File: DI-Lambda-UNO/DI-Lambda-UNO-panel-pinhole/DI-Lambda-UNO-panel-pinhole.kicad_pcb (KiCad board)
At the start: 2 copper layers, 33.2 x 26.6 mm, 1 part

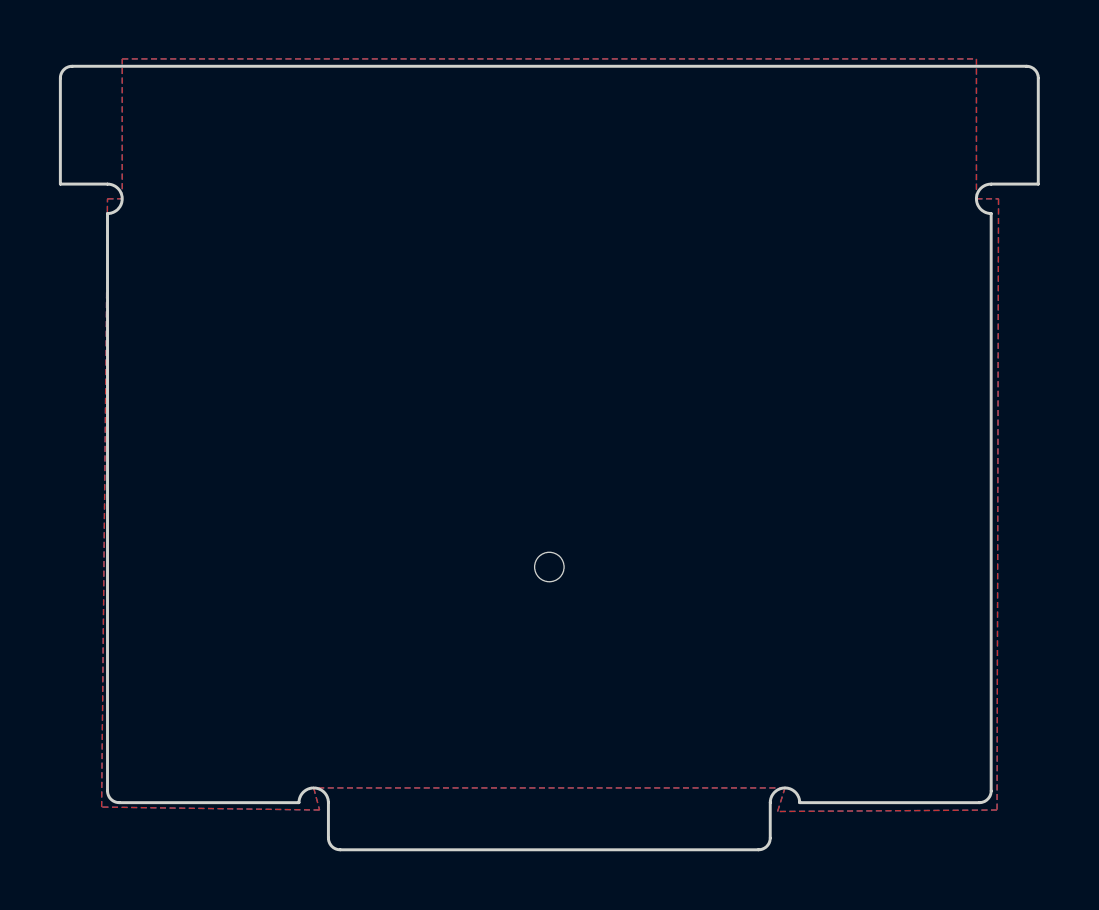
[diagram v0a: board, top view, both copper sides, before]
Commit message: Pinhole board: Convert to 18mm height
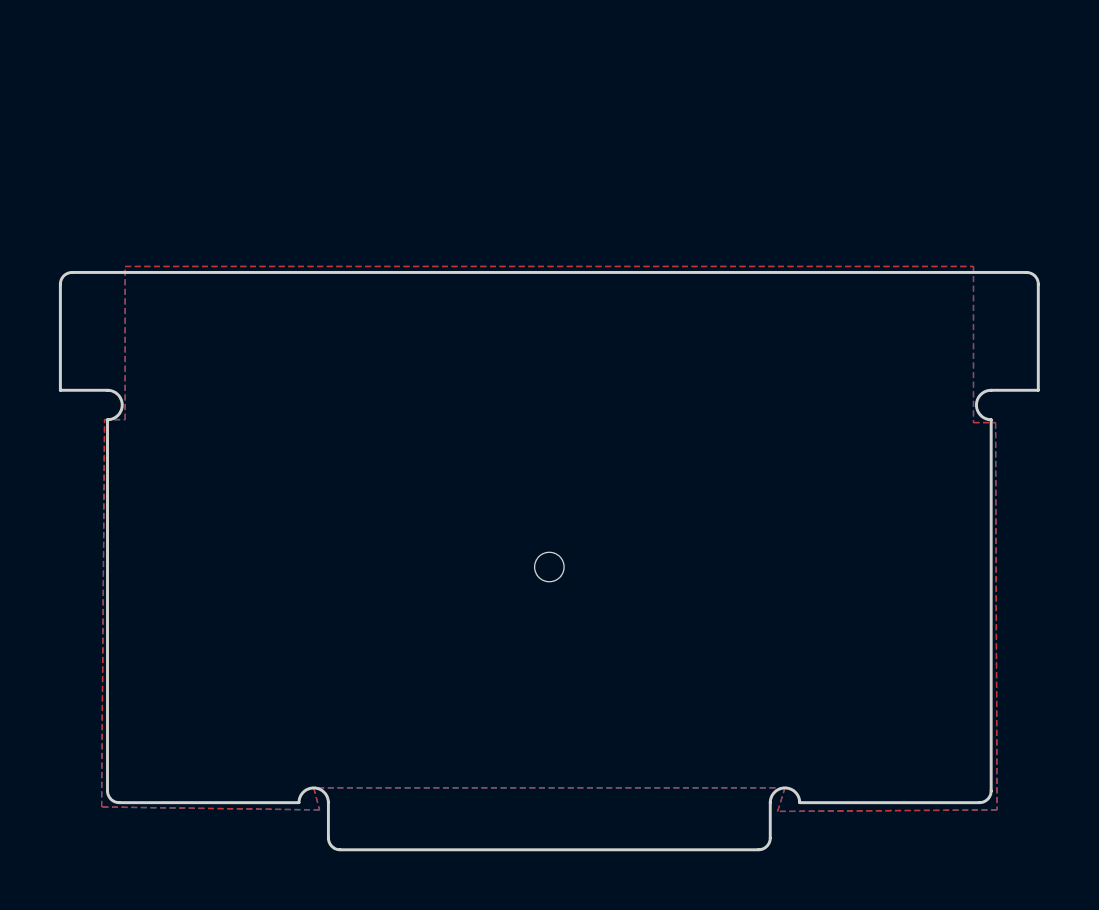
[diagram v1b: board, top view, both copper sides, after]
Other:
- board size 33.2 x 26.6 mm -> 33.2 x 19.6 mm
- board text added: "DI-Lambda UNO v1.3"
- board text removed: "DI-Lambda UNO v1.1"
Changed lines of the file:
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@@
     (pad "" np_thru_hole circle (at 0 0) (size 1 1) (drill 1) (layers *.Cu))
   )
-  (gr_text "DI-Lambda UNO v1.1" (at 160 70.8) (layer F.Mask)
+  (gr_text "DI-Lambda UNO v1.3" (at 160.2 76.4) (layer F.Mask)
     (effects (font (size 1.5 1.5) (thickness 0.3)))
   )
@@
     (arrow2b (pts (xy 156.2 92) (xy 155.613579 90.873496)))
   )
-  (gr_arc (start 175 71.5) (end 175 72) (angle 180) (layer Edge.Cuts) (width 0.1))
-  (gr_arc (start 145 71.5) (end 145 71) (angle 180) (layer Edge.Cuts) (width 0.1))
-  (gr_arc (start 176.2 67.4) (end 176.2 67) (angle 90) (layer Edge.Cuts) (width 0.1))
-  (gr_arc (start 143.8 67.4) (end 143.4 67.4) (angle 90) (layer Edge.Cuts) (width 0.1))
+  (gr_arc (start 175 78.5) (end 175 79) (angle 180) (layer Edge.Cuts) (width 0.1))
+  (gr_arc (start 145 78.5) (end 145 78) (angle 180) (layer Edge.Cuts) (width 0.1))
+  (gr_arc (start 176.2 74.4) (end 176.2 74) (angle 90) (layer Edge.Cuts) (width 0.1))
+  (gr_arc (start 143.8 74.4) (end 143.4 74.4) (angle 90) (layer Edge.Cuts) (width 0.1))
   (gr_arc (start 174.6 91.6) (end 175 91.6) (angle 90) (layer Edge.Cuts) (width 0.1))
   (gr_arc (start 145.4 91.6) (end 145.4 92) (angle 90) (layer Edge.Cuts) (width 0.1))
@@
   (gr_arc (start 168 92) (end 167.5 92) (angle 180) (layer Edge.Cuts) (width 0.1))
   (gr_arc (start 152 92) (end 151.5 92) (angle 180) (layer Edge.Cuts) (width 0.1))
-  (gr_line (start 175 91.6) (end 175 72) (layer Edge.Cuts) (width 0.1))
-  (gr_line (start 176.2 67) (end 143.8 67) (layer Edge.Cuts) (width 0.1))
-  (gr_line (start 175 71) (end 176.6 71) (layer Edge.Cuts) (width 0.1))
-  (gr_line (start 145 91.6) (end 145 72) (layer Edge.Cuts) (width 0.1))
+  (gr_line (start 175 91.6) (end 175 79) (layer Edge.Cuts) (width 0.1))
+  (gr_line (start 176.2 74) (end 143.8 74) (layer Edge.Cuts) (width 0.1))
+  (gr_line (start 175 78) (end 176.6 78) (layer Edge.Cuts) (width 0.1))
+  (gr_line (start 145 91.6) (end 145 79) (layer Edge.Cuts) (width 0.1))
   (gr_line (start 174.6 92) (end 168.5 92) (layer Edge.Cuts) (width 0.1))
-  (gr_line (start 176.6 67.4) (end 176.6 71) (layer Edge.Cuts) (width 0.1))
+  (gr_line (start 176.6 74.4) (end 176.6 78) (layer Edge.Cuts) (width 0.1))
   (gr_line (start 167.5 93.2) (end 167.5 92) (layer Edge.Cuts) (width 0.1))
   (gr_line (start 152.9 93.6) (end 167.1 93.6) (layer Edge.Cuts) (width 0.1))
-  (gr_line (start 143.4 71) (end 143.4 67.4) (layer Edge.Cuts) (width 0.1))
-  (gr_line (start 145 71) (end 143.4 71) (layer Edge.Cuts) (width 0.1))
+  (gr_line (start 143.4 78) (end 143.4 74.4) (layer Edge.Cuts) (width 0.1))
+  (gr_line (start 145 78) (end 143.4 78) (layer Edge.Cuts) (width 0.1))
   (gr_line (start 152.5 92) (end 152.5 93.2) (layer Edge.Cuts) (width 0.1))
   (gr_line (start 145.4 92) (end 151.5 92) (layer Edge.Cuts) (width 0.1))
-  (zone (net 0) (net_name "") (layer F.Cu) (hatch edge 0.508)
-    (connect_pads (clearance 0.508))
-    (min_thickness 0.254)
-    (fill yes (arc_segments 16) (thermal_gap 0.508) (thermal_bridge_width 0.508))
-    (polygon
-      (pts
-        (xy 145.5 66.75) (xy 174.5 66.75) (xy 174.5 71.5) (xy 175.25 71.5) (xy 175.2 92.25)
-        (xy 167.75 92.3) (xy 168 91.5) (xy 152 91.5) (xy 152.2 92.25) (xy 144.8 92.15)
-        (xy 145 71.5) (xy 145.5 71.5)
-      )
-    )
-  )
   (zone (net 0) (net_name "") (layer B.Cu) (hatch edge 0.508)
     (connect_pads (clearance 0.508))
@@
     (polygon
       (pts
-        (xy 145.5 66.75) (xy 174.5 66.75) (xy 174.5 71.5) (xy 175.25 71.5) (xy 175.2 92.25)
+        (xy 145.6 73.8) (xy 174.4 73.8) (xy 174.4 79.1) (xy 175.15 79.1) (xy 175.2 92.25)
         (xy 167.75 92.3) (xy 168 91.5) (xy 152 91.5) (xy 152.2 92.25) (xy 144.8 92.15)
-        (xy 145 71.5) (xy 145.5 71.5)
+        (xy 144.9 79) (xy 145.6 79)
       )
     )
@@
     (polygon
       (pts
-        (xy 147.5 69.5) (xy 172.25 69.5) (xy 172.25 72) (xy 147.5 72)
+        (xy 147.7 75.1) (xy 172.45 75.1) (xy 172.45 77.6) (xy 147.7 77.6)
       )
     )
+  )
+  (zone (net 0) (net_name "") (layer F.Cu) (hatch edge 0.508)
+    (connect_pads (clearance 0.508))
+    (min_thickness 0.254)
+    (fill yes (arc_segments 16) (thermal_gap 0.508) (thermal_bridge_width 0.508))
+    (polygon
+      (pts
+        (xy 145.6 73.792794) (xy 174.4 73.792794) (xy 174.4 79.092794) (xy 175.15 79.092794) (xy 175.2 92.242794)
+        (xy 167.75 92.292794) (xy 168 91.492794) (xy 152 91.492794) (xy 152.2 92.242794) (xy 144.8 92.142794)
+        (xy 144.9 78.992794) (xy 145.6 78.992794)
+      )
+    )

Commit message: Version 1.5
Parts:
- added MK2: Mounting_Hole, DI-Lambda-module-tabs:Tab_PINHOLE, F.Cu at (160.0, 92.0)
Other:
- board size 33.2 x 19.6 mm -> 33.2 x 25 mm
- board text added: "DI-Lambda UNO v1.5"
- board text removed: "DI-Lambda UNO v1.3"
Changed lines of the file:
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@@
-(kicad_pcb (version 20170123) (host pcbnew "(2017-09-07 revision 3b08636)-master")
+(kicad_pcb (version 20171130) (host pcbnew "(2018-01-22 revision c702646)-master")
   (general
     (thickness 1.6)
-    (drawings 26)
+    (drawings 19)
     (tracks 0)
     (zones 0)
-    (modules 1)
+    (modules 2)
     (nets 1)
   )
@@
       (layerselection 0x010f0_ffffffff)
       (usegerberextensions true)
-      (usegerberattributes true)
-      (usegerberadvancedattributes true)
+      (usegerberattributes false)
+      (usegerberadvancedattributes false)
       (creategerberjobfile true)
-      (excludeedgelayer false)
+      (excludeedgelayer true)
       (linewidth 0.100000)
       (plotframeref false)
@@
       (drillshape 0)
       (scaleselection 1)
-      (outputdirectory DI-Lambda-UNO-panel-pinhole-v1.1-gerbers-2017oct25/))
+      (outputdirectory DI-Lambda-UNO-panel-pinhole-v1.5-gerbers-2018feb07-1))
   )
   (net 0 "")
@@
     (uvia_drill 0.1)
   )
+  (module DI-Lambda-module-tabs:Tab_PINHOLE (layer F.Cu)
+    (at 160 92)
+    (fp_text reference MK2 (at 0 5.75) (layer F.SilkS) hide
+      (effects (font (size 1 1) (thickness 0.15)))
+    )
+    (fp_text value Mounting_Hole (at 0 3.5) (layer F.Fab)
+      (effects (font (size 1 1) (thickness 0.15)))
+    )
+    (fp_line (start -15 -2.5) (end -15 2.5) (layer F.Fab) (width 0.1))
+    (fp_line (start 15 -2.5) (end 15 2.5) (layer F.Fab) (width 0.1))
+    (fp_line (start -4.5 1.5) (end 4.5 1.5) (layer Edge.Cuts) (width 0.15))
+    (fp_line (start 5 1) (end 5 0) (layer Edge.Cuts) (width 0.15))
+    (fp_line (start -5 1) (end -5 0) (layer Edge.Cuts) (width 0.15))
+    (fp_arc (start -4.5 1) (end -5 1) (angle -90) (layer Edge.Cuts) (width 0.15))
+    (fp_arc (start 4.5 1) (end 4.5 1.5) (angle -90) (layer Edge.Cuts) (width 0.15))
+    (fp_arc (start -5.75 0) (end -5 0) (angle -180) (layer Edge.Cuts) (width 0.15))
+    (fp_arc (start 5.75 0) (end 6.5 0) (angle -180) (layer Edge.Cuts) (width 0.15))
+    (fp_line (start -5 -1) (end -5 2) (layer F.Fab) (width 0.1))
+    (fp_line (start 5 -1) (end 5 2) (layer F.Fab) (width 0.1))
+  )
   (module 1mm_hole:NPTH_1mm (layer F.Cu)
     (at 160 84)
@@
     (pad "" np_thru_hole circle (at 0 0) (size 1 1) (drill 1) (layers *.Cu))
   )
-  (gr_text "DI-Lambda UNO v1.3" (at 160.2 76.4) (layer F.Mask)
+  (gr_text "DI-Lambda UNO v1.5" (at 160.2 69.4) (layer F.Mask)
     (effects (font (size 1.5 1.5) (thickness 0.3)))
   )
@@
     (arrow2b (pts (xy 156.2 92) (xy 155.613579 90.873496)))
   )
-  (gr_arc (start 175 78.5) (end 175 79) (angle 180) (layer Edge.Cuts) (width 0.1))
-  (gr_arc (start 145 78.5) (end 145 78) (angle 180) (layer Edge.Cuts) (width 0.1))
-  (gr_arc (start 176.2 74.4) (end 176.2 74) (angle 90) (layer Edge.Cuts) (width 0.1))
-  (gr_arc (start 143.8 74.4) (end 143.4 74.4) (angle 90) (layer Edge.Cuts) (width 0.1))
+  (gr_arc (start 175 71.5) (end 175 72) (angle 180) (layer Edge.Cuts) (width 0.1))
+  (gr_arc (start 145 71.5) (end 145 71) (angle 180) (layer Edge.Cuts) (width 0.1))
+  (gr_arc (start 176.2 67.4) (end 176.2 67) (angle 90) (layer Edge.Cuts) (width 0.1))
+  (gr_arc (start 143.8 67.4) (end 143.4 67.4) (angle 90) (layer Edge.Cuts) (width 0.1))
   (gr_arc (start 174.6 91.6) (end 175 91.6) (angle 90) (layer Edge.Cuts) (width 0.1))
   (gr_arc (start 145.4 91.6) (end 145.4 92) (angle 90) (layer Edge.Cuts) (width 0.1))
-  (gr_arc (start 167.1 93.2) (end 167.5 93.2) (angle 90) (layer Edge.Cuts) (width 0.1))
-  (gr_arc (start 152.9 93.2) (end 152.9 93.6) (angle 90) (layer Edge.Cuts) (width 0.1))
-  (gr_arc (start 168 92) (end 167.5 92) (angle 180) (layer Edge.Cuts) (width 0.1))
-  (gr_arc (start 152 92) (end 151.5 92) (angle 180) (layer Edge.Cuts) (width 0.1))
-  (gr_line (start 175 91.6) (end 175 79) (layer Edge.Cuts) (width 0.1))
-  (gr_line (start 176.2 74) (end 143.8 74) (layer Edge.Cuts) (width 0.1))
-  (gr_line (start 175 78) (end 176.6 78) (layer Edge.Cuts) (width 0.1))
-  (gr_line (start 145 91.6) (end 145 79) (layer Edge.Cuts) (width 0.1))
-  (gr_line (start 174.6 92) (end 168.5 92) (layer Edge.Cuts) (width 0.1))
-  (gr_line (start 176.6 74.4) (end 176.6 78) (layer Edge.Cuts) (width 0.1))
-  (gr_line (start 167.5 93.2) (end 167.5 92) (layer Edge.Cuts) (width 0.1))
-  (gr_line (start 152.9 93.6) (end 167.1 93.6) (layer Edge.Cuts) (width 0.1))
-  (gr_line (start 143.4 78) (end 143.4 74.4) (layer Edge.Cuts) (width 0.1))
-  (gr_line (start 145 78) (end 143.4 78) (layer Edge.Cuts) (width 0.1))
-  (gr_line (start 152.5 92) (end 152.5 93.2) (layer Edge.Cuts) (width 0.1))
-  (gr_line (start 145.4 92) (end 151.5 92) (layer Edge.Cuts) (width 0.1))
+  (gr_line (start 175 91.6) (end 175 72) (layer Edge.Cuts) (width 0.1))
+  (gr_line (start 176.2 67) (end 143.8 67) (layer Edge.Cuts) (width 0.1))
+  (gr_line (start 175 71) (end 176.6 71) (layer Edge.Cuts) (width 0.1))
+  (gr_line (start 145 91.6) (end 145 72) (layer Edge.Cuts) (width 0.1))
+  (gr_line (start 174.6 92) (end 166.5 92) (layer Edge.Cuts) (width 0.1))
+  (gr_line (start 176.6 67.4) (end 176.6 71) (layer Edge.Cuts) (width 0.1))
+  (gr_line (start 143.4 71) (end 143.4 67.4) (layer Edge.Cuts) (width 0.1))
+  (gr_line (start 145 71) (end 143.4 71) (layer Edge.Cuts) (width 0.1))
+  (gr_line (start 145.4 92) (end 153.5 92) (layer Edge.Cuts) (width 0.1))
   (zone (net 0) (net_name "") (layer B.Cu) (hatch edge 0.508)
     (connect_pads (clearance 0.508))
@@
     (polygon
       (pts
-        (xy 145.6 73.8) (xy 174.4 73.8) (xy 174.4 79.1) (xy 175.15 79.1) (xy 175.2 92.25)
+        (xy 145.6 66.4) (xy 174.45 66.55) (xy 174.45 71.5) (xy 175.2 71.5) (xy 175.2 92.25)
         (xy 167.75 92.3) (xy 168 91.5) (xy 152 91.5) (xy 152.2 92.25) (xy 144.8 92.15)
-        (xy 144.9 79) (xy 145.6 79)
+        (xy 144.9 71.5) (xy 145.6 71.5)
       )
     )
@@
     (polygon
       (pts
-        (xy 147.7 75.1) (xy 172.45 75.1) (xy 172.45 77.6) (xy 147.7 77.6)
+        (xy 147.7 68.1) (xy 172.45 68.1) (xy 172.45 70.6) (xy 147.7 70.6)
       )
     )
@@
     (polygon
       (pts
-        (xy 145.6 73.792794) (xy 174.4 73.792794) (xy 174.4 79.092794) (xy 175.15 79.092794) (xy 175.2 92.242794)
+        (xy 145.65 66.55) (xy 174.45 66.55) (xy 174.45 71.5) (xy 175.2 71.5) (xy 175.2 92.242794)
         (xy 167.75 92.292794) (xy 168 91.492794) (xy 152 91.492794) (xy 152.2 92.242794) (xy 144.8 92.142794)
-        (xy 144.9 78.992794) (xy 145.6 78.992794)
+        (xy 144.95 71.5) (xy 145.65 71.5)
       )
     )

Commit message: More missing fotprints
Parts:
- moved MK1 158.3 mm to (16.6, 17.0)
- moved MK2 158.3 mm to (16.6, 25.0)
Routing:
- net (no net): vias 0 -> 1
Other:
- board text added: "DI-Lambda UNO v1.7"
- board text removed: "DI-Lambda UNO v1.5"
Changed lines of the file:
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@@
-(kicad_pcb (version 20171130) (host pcbnew "(2018-01-22 revision c702646)-master")
+(kicad_pcb (version 20171130) (host pcbnew "(5.0.0-rc2-dev-425-g1663627)")
   (general
     (thickness 1.6)
     (drawings 19)
-    (tracks 0)
+    (tracks 1)
     (zones 0)
     (modules 2)
@@
     (pad_drill 1)
     (pad_to_mask_clearance 0.2)
-    (aux_axis_origin 143.4 67)
-    (grid_origin 145 92)
+    (aux_axis_origin 0 0)
     (visible_elements FFFFFF7F)
     (pcbplotparams
@@
   )
   (module DI-Lambda-module-tabs:Tab_PINHOLE (layer F.Cu)
-    (at 160 92)
+    (at 16.6 25)
     (fp_text reference MK2 (at 0 5.75) (layer F.SilkS) hide
       (effects (font (size 1 1) (thickness 0.15)))
@@
   )
   (module 1mm_hole:NPTH_1mm (layer F.Cu)
-    (at 160 84)
+    (at 16.6 17)
     (fp_text reference MK1 (at 0 3.5) (layer F.SilkS) hide
       (effects (font (size 1 1) (thickness 0.15)))
@@
     (pad "" np_thru_hole circle (at 0 0) (size 1 1) (drill 1) (layers *.Cu))
   )
-  (gr_text "DI-Lambda UNO v1.5" (at 160.2 69.4) (layer F.Mask)
+  (gr_text "DI-Lambda UNO v1.7" (at 16.8 2.4) (layer F.Mask)
     (effects (font (size 1.5 1.5) (thickness 0.3)))
   )
@@
     (arrow2b (pts (xy 156.2 92) (xy 155.613579 90.873496)))
   )
-  (gr_arc (start 175 71.5) (end 175 72) (angle 180) (layer Edge.Cuts) (width 0.1))
-  (gr_arc (start 145 71.5) (end 145 71) (angle 180) (layer Edge.Cuts) (width 0.1))
-  (gr_arc (start 176.2 67.4) (end 176.2 67) (angle 90) (layer Edge.Cuts) (width 0.1))
-  (gr_arc (start 143.8 67.4) (end 143.4 67.4) (angle 90) (layer Edge.Cuts) (width 0.1))
-  (gr_arc (start 174.6 91.6) (end 175 91.6) (angle 90) (layer Edge.Cuts) (width 0.1))
-  (gr_arc (start 145.4 91.6) (end 145.4 92) (angle 90) (layer Edge.Cuts) (width 0.1))
-  (gr_line (start 175 91.6) (end 175 72) (layer Edge.Cuts) (width 0.1))
-  (gr_line (start 176.2 67) (end 143.8 67) (layer Edge.Cuts) (width 0.1))
-  (gr_line (start 175 71) (end 176.6 71) (layer Edge.Cuts) (width 0.1))
-  (gr_line (start 145 91.6) (end 145 72) (layer Edge.Cuts) (width 0.1))
-  (gr_line (start 174.6 92) (end 166.5 92) (layer Edge.Cuts) (width 0.1))
-  (gr_line (start 176.6 67.4) (end 176.6 71) (layer Edge.Cuts) (width 0.1))
-  (gr_line (start 143.4 71) (end 143.4 67.4) (layer Edge.Cuts) (width 0.1))
-  (gr_line (start 145 71) (end 143.4 71) (layer Edge.Cuts) (width 0.1))
-  (gr_line (start 145.4 92) (end 153.5 92) (layer Edge.Cuts) (width 0.1))
+  (gr_arc (start 31.6 4.5) (end 31.6 5) (angle 180) (layer Edge.Cuts) (width 0.1))
+  (gr_arc (start 1.6 4.5) (end 1.6 4) (angle 180) (layer Edge.Cuts) (width 0.1))
+  (gr_arc (start 32.8 0.4) (end 32.8 0) (angle 90) (layer Edge.Cuts) (width 0.1))
+  (gr_arc (start 0.4 0.4) (end 0 0.4) (angle 90) (layer Edge.Cuts) (width 0.1))
+  (gr_arc (start 31.2 24.6) (end 31.6 24.6) (angle 90) (layer Edge.Cuts) (width 0.1))
+  (gr_arc (start 2 24.6) (end 2 25) (angle 90) (layer Edge.Cuts) (width 0.1))
+  (gr_line (start 31.6 24.6) (end 31.6 5) (layer Edge.Cuts) (width 0.1))
+  (gr_line (start 32.8 0) (end 0.4 0) (layer Edge.Cuts) (width 0.1))
+  (gr_line (start 31.6 4) (end 33.2 4) (layer Edge.Cuts) (width 0.1))
+  (gr_line (start 1.6 24.6) (end 1.6 5) (layer Edge.Cuts) (width 0.1))
+  (gr_line (start 31.2 25) (end 23.1 25) (layer Edge.Cuts) (width 0.1))
+  (gr_line (start 33.2 0.4) (end 33.2 4) (layer Edge.Cuts) (width 0.1))
+  (gr_line (start 0 4) (end 0 0.4) (layer Edge.Cuts) (width 0.1))
+  (gr_line (start 1.6 4) (end 0 4) (layer Edge.Cuts) (width 0.1))
+  (gr_line (start 2 25) (end 10.1 25) (layer Edge.Cuts) (width 0.1))
+  (via (at 0 0) (size 0.8) (drill 0.4) (layers F.Cu B.Cu) (net 0))
   (zone (net 0) (net_name "") (layer B.Cu) (hatch edge 0.508)
     (connect_pads (clearance 0.508))
@@
     (polygon
       (pts
-        (xy 145.6 66.4) (xy 174.45 66.55) (xy 174.45 71.5) (xy 175.2 71.5) (xy 175.2 92.25)
-        (xy 167.75 92.3) (xy 168 91.5) (xy 152 91.5) (xy 152.2 92.25) (xy 144.8 92.15)
-        (xy 144.9 71.5) (xy 145.6 71.5)
+        (xy 2.2 -0.6) (xy 31.05 -0.45) (xy 31.05 4.5) (xy 31.8 4.5) (xy 31.8 25.25)
+        (xy 24.35 25.3) (xy 24.6 24.5) (xy 8.6 24.5) (xy 8.8 25.25) (xy 1.4 25.15)
+        (xy 1.5 4.5) (xy 2.2 4.5)
       )
     )
@@
     (polygon
       (pts
-        (xy 147.7 68.1) (xy 172.45 68.1) (xy 172.45 70.6) (xy 147.7 70.6)
+        (xy 4.3 1.1) (xy 29.05 1.1) (xy 29.05 3.6) (xy 4.3 3.6)
       )
     )
@@
     (polygon
       (pts
-        (xy 145.65 66.55) (xy 174.45 66.55) (xy 174.45 71.5) (xy 175.2 71.5) (xy 175.2 92.242794)
-        (xy 167.75 92.292794) (xy 168 91.492794) (xy 152 91.492794) (xy 152.2 92.242794) (xy 144.8 92.142794)
-        (xy 144.95 71.5) (xy 145.65 71.5)
+        (xy 2.25 -0.45) (xy 31.05 -0.45) (xy 31.05 4.5) (xy 31.8 4.5) (xy 31.8 25.242794)
+        (xy 24.35 25.292794) (xy 24.6 24.492794) (xy 8.6 24.492794) (xy 8.8 25.242794) (xy 1.4 25.142794)
+        (xy 1.55 4.5) (xy 2.25 4.5)
       )
     )
